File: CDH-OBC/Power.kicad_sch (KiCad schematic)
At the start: 0 parts

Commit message: finished bulk of the schematic
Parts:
- added C13: 10uF, symbol Device:C_Small
- added C14, C15: 22uF, symbol Device:C_Small
- added C16, C25: 100nF, symbol Device:C_Small
- added C17: 1uF, symbol Device:C_Small
- added C18, C19, C24: 4.7uF, symbol Device:C_Small
- added D2, D4, D5: LED, symbol Device:LED
- added D3: SMAJ18CA, Diode_SMD:D_SMA, symbol Diode:SMAJ18CA
- added F1: Fuse, symbol Device:Fuse
- added J2: BAT, symbol Connector_Generic:Conn_01x02
- added J4: Molex 6 pin, symbol Connector_Generic:Conn_01x06
- added L1: 4.7uH, symbol Device:L_Small
- added L2: BLM21PG221SN1D, symbol Device:L
- added MOSFET1: SSM3K324R_LF, SOT-23F_TOS, symbol OBC-lib:SSM3K324R_LF
- added Q1: PMOS, symbol Simulation_SPICE:PMOS
- added R16, R17, R18, R22: 10k, symbol Device:R_Small_US
- added R19: 100k, symbol Device:R_Small_US
- added R20, R23: 1k, symbol Device:R_Small_US
- added R21: 52k, symbol Device:R_Small_US
- added R24: 470, symbol Device:R_Small_US
- added SW3: slide SW, symbol Switch:SW_SPST
- added TP8, TP9: TestPoint, symbol Connector:TestPoint
- added U10: MCP1826S, symbol Regulator_Linear:MCP1826S
- added U8: AP63205WU, Package_TO_SOT_SMD:TSOT-23-6, symbol Regulator_Switching:AP63205WU
- added U9: MIC37300-3.3WR, SPAK-3LD-PL-1_MCH, symbol OBC-lib:MIC37300-3.3WR
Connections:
- new net: F1.2, SW3.1 (A)
- new net: MOSFET1.3, R19.2, U8.2 (EN)
- new net: Q1.2 (G), R17.1, R18.1
- new net: F1.1, Q1.3 (S), R18.2
- new net: D5.2 (A), R24.2
- new net: D4.2 (A), R23.2
- new net: C19.1, TP9.1, U9.3 (VOUT)
- new net: C16.1, L1.1, U8.5 (SW)
- new net: C16.2, U8.6 (BST)
- new net: D2.2 (A), R16.2
- new net +1V2: C17.1, U10.3 (VO)
- new net +3V3: C18.1, J4.3 (Pin_3), J4.4 (Pin_4), L2.1, R24.1, U10.1 (VI)
- new net +5F: R23.1
- new net +5V: C14.1, C14.2, C15.1, C15.2, J4.1 (Pin_1), J4.2 (Pin_2), L1.2, TP8.1, U8.1 (FB), U9.1 (VIN)
- new net ADREFHI: C24.1, C25.1, L2.2
- new net BUCK_EN: MOSFET1.1, R20.1
- new net GND: C13.2, C17.2, C18.2, C19.2, C24.2, C25.2, D2.1 (K), D3.1 (A1), D4.1 (K), D5.1 (K), J2.2 (Pin_2), J4.5 (Pin_5), J4.6 (Pin_6), MOSFET1.2, R17.2, R20.2, R22.2, U10.2 (GND), U8.4 (GND), U9.2 (GND), U9.4 (GND)
- new net VBAT: D3.2 (A2), J2.1 (Pin_1), Q1.1 (D), R16.1
- new net VBAT_monitoring: R21.2, R22.1
- new net VBUS: C13.1, R19.1, R21.1, SW3.2 (B), U8.3 (IN)
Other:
- note added: "Voltage Divider: 16.8V * 10/62.3 ~ 2.7V max"

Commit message: finished schematic
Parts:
- C13, C14, C15, C16, C17, C18, C19, C24, C25: footprint (none) -> Capacitor_SMD:C_0603_1608Metric
- D2, D4, D5: footprint (none) -> LED_SMD:LED_0603_1608Metric
- F1: footprint (none) -> Fuse:Fuse_0805_2012Metric
- J2: footprint (none) -> Connector_AMASS:AMASS_XT60IPW-M_1x03_P7.20mm_Horizontal
- J4: footprint (none) -> Connector_Molex:Molex_Micro-Fit_3.0_43045-0600_2x03_P3.00mm_Horizontal
- L1: footprint (none) -> Inductor_SMD:L_Sunlord_SWPA5040S
- L2: footprint (none) -> Inductor_SMD:L_0805_2012Metric
- Q1: footprint (none) -> Package_TO_SOT_SMD:TSOT-23
- R16, R17, R18, R19, R20, R21, R22, R23, R24: footprint (none) -> Resistor_SMD:R_0603_1608Metric
- TP8, TP9: footprint (none) -> TestPoint:TestPoint_Pad_D1.0mm
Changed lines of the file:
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@@
 			)
 		)
-		(property "Footprint" ""
+		(property "Footprint" "Resistor_SMD:R_0603_1608Metric"
 			(at 92.71 67.31 0)
 			(hide yes)
@@
 			)
 		)
-		(property "Footprint" ""
+		(property "Footprint" "LED_SMD:LED_0603_1608Metric"
 			(at 158.75 184.15 0)
 			(hide yes)
@@
 			)
 		)
-		(property "Footprint" ""
+		(property "Footprint" "Capacitor_SMD:C_0603_1608Metric"
 			(at 102.87 161.29 0)
 			(hide yes)
@@
 			)
 		)
-		(property "Footprint" ""
+		(property "Footprint" "Capacitor_SMD:C_0603_1608Metric"
 			(at 58.42 148.59 0)
 			(hide yes)
@@
 			)
 		)
-		(property "Footprint" ""
+		(property "Footprint" "Resistor_SMD:R_0603_1608Metric"
 			(at 85.09 71.12 0)
 			(hide yes)
@@
 			)
 		)
-		(property "Footprint" ""
+		(property "Footprint" "Resistor_SMD:R_0603_1608Metric"
 			(at 147.32 170.18 0)
 			(hide yes)
@@
 			)
 		)
-		(property "Footprint" ""
+		(property "Footprint" "Capacitor_SMD:C_0603_1608Metric"
 			(at 120.65 113.03 0)
 			(hide yes)
@@
 			)
 		)
-		(property "Footprint" ""
+		(property "Footprint" "TestPoint:TestPoint_Pad_D1.0mm"
 			(at 68.58 115.57 0)
 			(hide yes)
@@
 			)
 		)
-		(property "Footprint" ""
+		(property "Footprint" "Resistor_SMD:R_0603_1608Metric"
 			(at 147.32 184.15 0)
 			(hide yes)
@@
 			)
 		)
-		(property "Footprint" ""
+		(property "Footprint" "Capacitor_SMD:C_0603_1608Metric"
 			(at 95.25 113.03 0)
 			(hide yes)
@@
 			)
 		)
-		(property "Footprint" ""
+		(property "Footprint" "Capacitor_SMD:C_0603_1608Metric"
 			(at 83.82 160.02 0)
 			(hide yes)
@@
 			)
 		)
-		(property "Footprint" ""
+		(property "Footprint" "Inductor_SMD:L_Sunlord_SWPA5040S"
 			(at 95.25 157.48 0)
 			(hide yes)
@@
 			)
 		)
-		(property "Footprint" ""
+		(property "Footprint" "Capacitor_SMD:C_0603_1608Metric"
 			(at 114.3 161.29 0)
 			(hide yes)
@@
 			)
 		)
-		(property "Footprint" ""
+		(property "Footprint" "Resistor_SMD:R_0603_1608Metric"
 			(at 29.21 181.61 0)
 			(hide yes)
@@
 			)
 		)
-		(property "Footprint" ""
+		(property "Footprint" "Inductor_SMD:L_0805_2012Metric"
 			(at 240.03 88.9 0)
 			(hide yes)
@@
 			)
 		)
-		(property "Footprint" ""
+		(property "Footprint" "TestPoint:TestPoint_Pad_D1.0mm"
 			(at 106.68 157.48 0)
 			(hide yes)
@@
 			)
 		)
-		(property "Footprint" ""
+		(property "Footprint" "Resistor_SMD:R_0603_1608Metric"
 			(at 241.3 143.51 0)
 			(hide yes)
@@
 			)
 		)
-		(property "Footprint" ""
+		(property "Footprint" "LED_SMD:LED_0603_1608Metric"
 			(at 49.53 71.12 0)
 			(hide yes)
@@
 			)
 		)
-		(property "Footprint" ""
+		(property "Footprint" "Resistor_SMD:R_0603_1608Metric"
 			(at 36.83 71.12 0)
 			(hide yes)
@@
 			)
 		)
-		(property "Footprint" ""
+		(property "Footprint" "Package_TO_SOT_SMD:TSOT-23"
 			(at 82.55 55.88 0)
 			(hide yes)
@@
 			)
 		)
-		(property "Footprint" ""
+		(property "Footprint" "Fuse:Fuse_0805_2012Metric"
 			(at 102.87 60.198 90)
 			(hide yes)
@@
 			)
 		)
-		(property "Footprint" ""
+		(property "Footprint" "Resistor_SMD:R_0603_1608Metric"
 			(at 45.72 160.02 0)
 			(hide yes)
@@
 			)
 		)
-		(property "Footprint" ""
+		(property "Footprint" "Capacitor_SMD:C_0603_1608Metric"
 			(at 261.62 93.98 0)
 			(hide yes)
@@
 			)
 		)
-		(property "Footprint" ""
+		(property "Footprint" "Resistor_SMD:R_0603_1608Metric"
 			(at 241.3 133.35 0)
 			(hide yes)
@@
 			)
 		)
-		(property "Footprint" ""
+		(property "Footprint" "Connector_Molex:Molex_Micro-Fit_3.0_43045-0600_2x03_P3.00mm_Horizontal"
 			(at 207.01 137.16 0)
 			(hide yes)
@@
 			)
 		)
-		(property "Footprint" ""
+		(property "Footprint" "Connector_AMASS:AMASS_XT60IPW-M_1x03_P7.20mm_Horizontal"
 			(at 21.59 76.2 0)
 			(hide yes)
@@
 			)
 		)
-		(property "Footprint" ""
+		(property "Footprint" "Capacitor_SMD:C_0603_1608Metric"
 			(at 68.58 115.57 0)
 			(hide yes)
@@
 			)
 		)
-		(property "Footprint" ""
+		(property "Footprint" "Capacitor_SMD:C_0603_1608Metric"
 			(at 246.38 93.98 0)
 			(hide yes)
@@
 			)
 		)
-		(property "Footprint" ""
+		(property "Footprint" "LED_SMD:LED_0603_1608Metric"
 			(at 158.75 170.18 0)
 			(hide yes)

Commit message: added some footprints
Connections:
- net GND: now also J2.1 (Pin_1); no longer J2.2 (Pin_2)
- net VBAT: now also J2.2 (Pin_2); no longer J2.1 (Pin_1)
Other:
- moved on the sheet: J2
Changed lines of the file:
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@@
 	(wire
 		(pts
-			(xy 26.67 78.74) (xy 26.67 80.01)
+			(xy 26.67 76.2) (xy 26.67 80.01)
 		)
 		(stroke
@@
 	(wire
 		(pts
+			(xy 26.67 73.66) (xy 26.67 71.12)
+		)
+		(stroke
+			(width 0)
+			(type default)
+		)
+	)
+	(wire
+		(pts
 			(xy 95.25 104.14) (xy 100.33 104.14)
 		)
@@
 	(wire
 		(pts
-			(xy 26.67 76.2) (xy 26.67 71.12)
-		)
-		(stroke
-			(width 0)
-			(type default)
-		)
-	)
-	(wire
-		(pts
 			(xy 246.38 88.9) (xy 261.62 88.9)
 		)
@@
 	(symbol
 		(lib_id "Connector_Generic:Conn_01x02")
-		(at 21.59 76.2 0)
-		(mirror y)
+		(at 21.59 76.2 180)
 		(unit 1)
 		(body_style 1)
@@
 		(in_pos_files yes)
 		(dnp no)
-		(fields_autoplaced yes)
 		(property "Reference" "J2"
-			(at 21.59 69.85 0)
+			(at 21.59 82.55 0)
 			(show_name no)
 			(do_not_autoplace no)
@@
 		)
 		(property "Value" "BAT"
-			(at 21.59 72.39 0)
+			(at 21.59 80.01 0)
 			(show_name no)
 			(do_not_autoplace no)

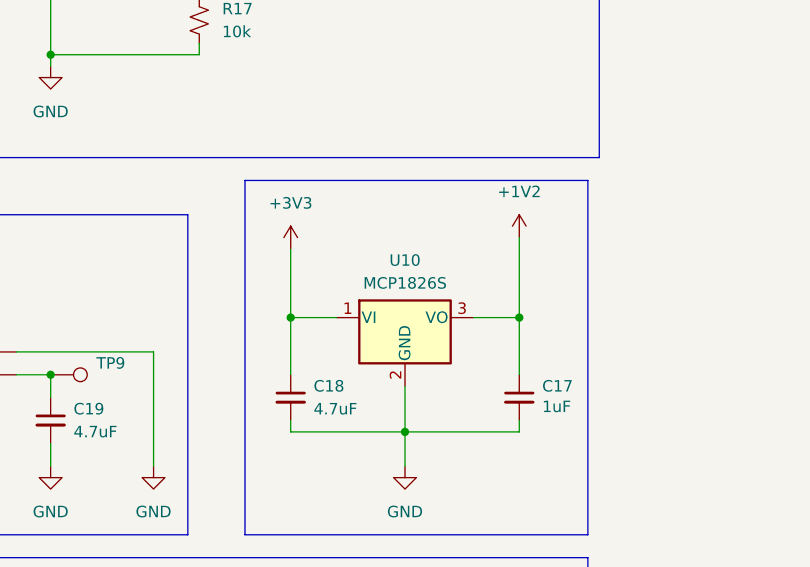
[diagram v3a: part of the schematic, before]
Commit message: finished adding footprints
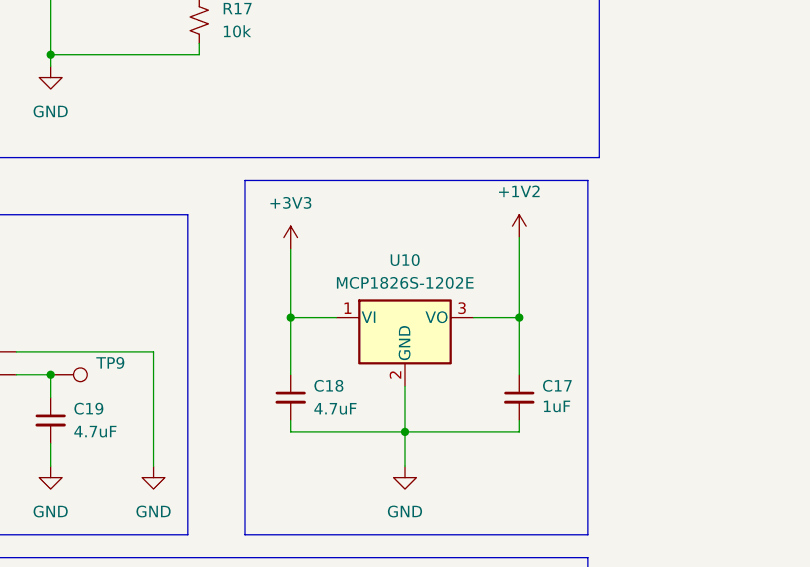
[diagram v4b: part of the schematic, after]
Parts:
- MOSFET1: footprint SOT-23F_TOS -> Package_TO_SOT_SMD:TSOT-23
- SW3: footprint (none) -> OBC-Lib:SW_GF-123-0054
- U10: value MCP1826S -> MCP1826S-1202E; footprint (none) -> OBC-Lib:SOT-223_3MC_MCH
- U9: footprint SPAK-3LD-PL-1_MCH -> OBC-Lib:SPAK-3LD-PL-1_MCH
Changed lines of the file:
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@@
 			)
 		)
-		(property "Footprint" ""
+		(property "Footprint" "OBC-Lib:SW_GF-123-0054"
 			(at 115.57 58.42 0)
 			(hide yes)
@@
 			)
 		)
-		(property "Footprint" "SOT-23F_TOS"
+		(property "Footprint" "Package_TO_SOT_SMD:TSOT-23"
 			(at 35.56 167.64 0)
 			(hide yes)
@@
 			)
 		)
-		(property "Value" "MCP1826S"
+		(property "Value" "MCP1826S-1202E"
 			(at 107.95 100.33 0)
 			(show_name no)
@@
 			)
 		)
-		(property "Footprint" ""
+		(property "Footprint" "OBC-Lib:SOT-223_3MC_MCH"
 			(at 105.41 100.33 0)
 			(hide yes)
@@
 			)
 		)
-		(property "Footprint" "SPAK-3LD-PL-1_MCH"
+		(property "Footprint" "OBC-Lib:SPAK-3LD-PL-1_MCH"
 			(at 24.13 107.95 0)
 			(hide yes)

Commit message: bulk schematic done
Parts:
- added TP13: TestPoint, TestPoint:TestPoint_Pad_D1.0mm, symbol Connector:TestPoint
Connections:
- net +5F is gone; now on net +5V: R23.1
- net +1V2: now also TP13.1
- net +3V3: now also C19.1, J4.2 (Pin_2), J4.5 (Pin_5), TP9.1, U9.3 (VOUT); no longer J4.3 (Pin_3), J4.4 (Pin_4)
- net +5V: now also J4.4 (Pin_4); no longer C14.2, C15.2, J4.2 (Pin_2), U8.1 (FB)
- net GND: now also J4.3 (Pin_3); no longer J4.5 (Pin_5)
- new net: C14.2, C15.2, U8.1 (FB)
